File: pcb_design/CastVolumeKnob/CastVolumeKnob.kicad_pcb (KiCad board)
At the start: 2 copper layers, 70 x 70 mm, 18 parts, among them J1 POWER_5V, J2 Conn_01x08, J3 NeoPixelRing, J4 Conn_01x08, J5 Encoder, J6 ATTINY85, Q1 2N7000, Q2 2N3904, Q3 IRF9540N, U1 WeMos_mini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

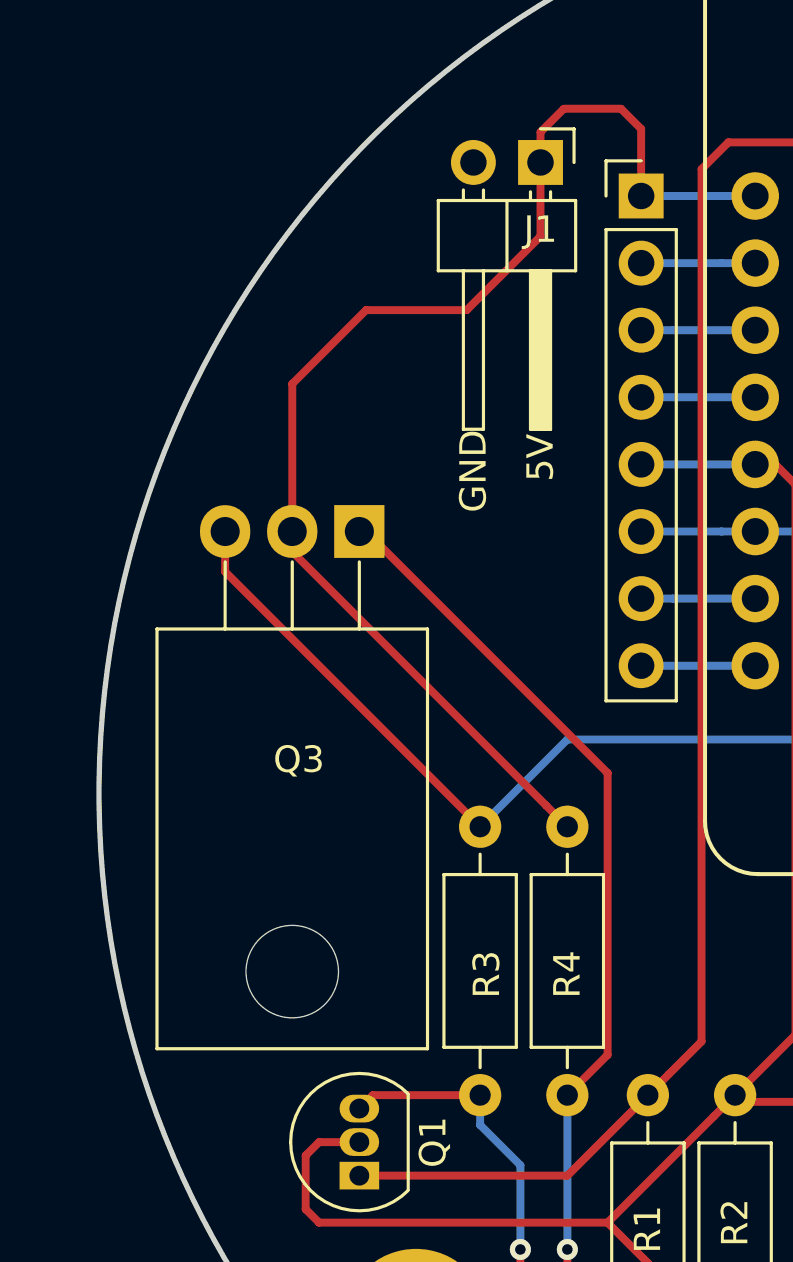
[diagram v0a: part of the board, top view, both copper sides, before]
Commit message: Fixed mosfet footprint for v2 pcb
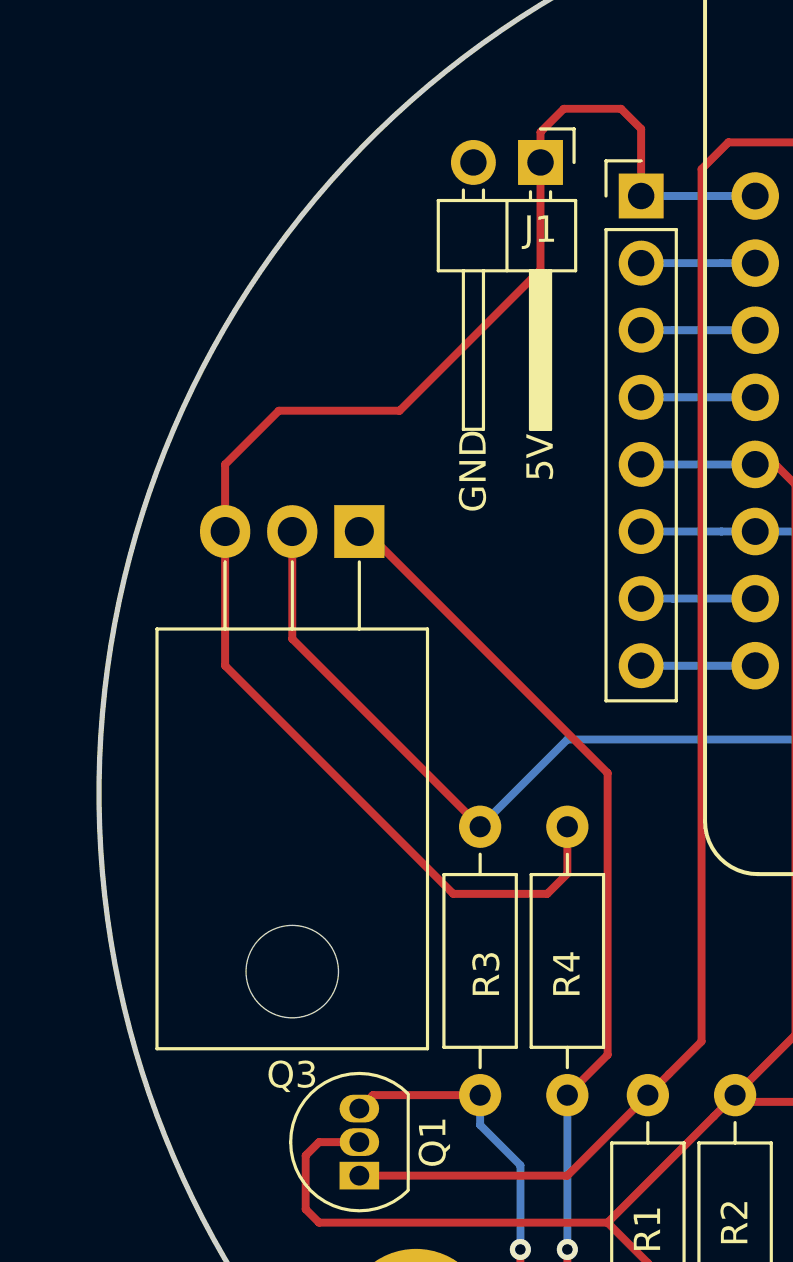
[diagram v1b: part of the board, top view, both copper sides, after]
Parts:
- Q3: footprint Package_TO_SOT_THT:TO-220-3_Horizontal_TabDown -> Package-TO:TO-220-3_Horizontal_TabDown-132
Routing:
- net +5V: track 48.1 -> 57.8 mm
